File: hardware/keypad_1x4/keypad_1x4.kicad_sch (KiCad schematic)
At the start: 11 parts, among them J1 Conn_01x04, J2 Conn_01x04, J3 Conn_01x01_Pin, J4 Conn_01x01_Pin, SW1 SW_Push_x4

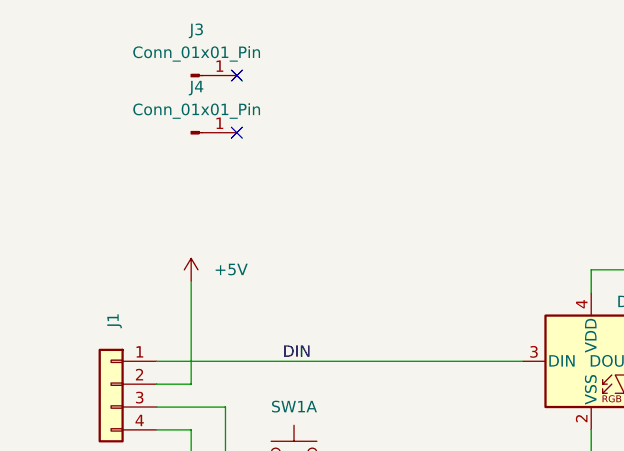
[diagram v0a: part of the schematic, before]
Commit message: Adding 1x2 LED illuminated keypad, updates to 1x4 board for gbrs
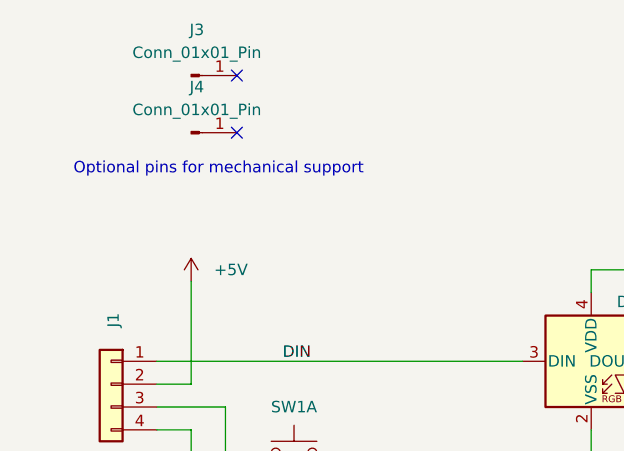
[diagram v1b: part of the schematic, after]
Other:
- note added: "Optional pins for mechanical support"
- company: (none) -> idyllm
- title: (none) -> 1x4 Neopixel Illuminated Keypad
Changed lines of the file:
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@@
 	(generator_version "9.0")
 	(paper "A4")
+	(title_block
+		(title "1x4 Neopixel Illuminated Keypad")
+		(date "2025-11-07")
+		(rev "1.0")
+		(company "idyllm")
+		(comment 1 "CC BY-SA 4.0")
+	)
+	(text "Optional pins for mechanical support"
+		(exclude_from_sim no)
+		(at 86.868 62.484 0)
+		(effects
+			(font
+				(size 1.27 1.27)
+			)
+		)
+	)
 	(junction
 		(at 100.33 101.6)
